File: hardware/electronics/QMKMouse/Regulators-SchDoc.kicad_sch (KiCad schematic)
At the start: 9 parts

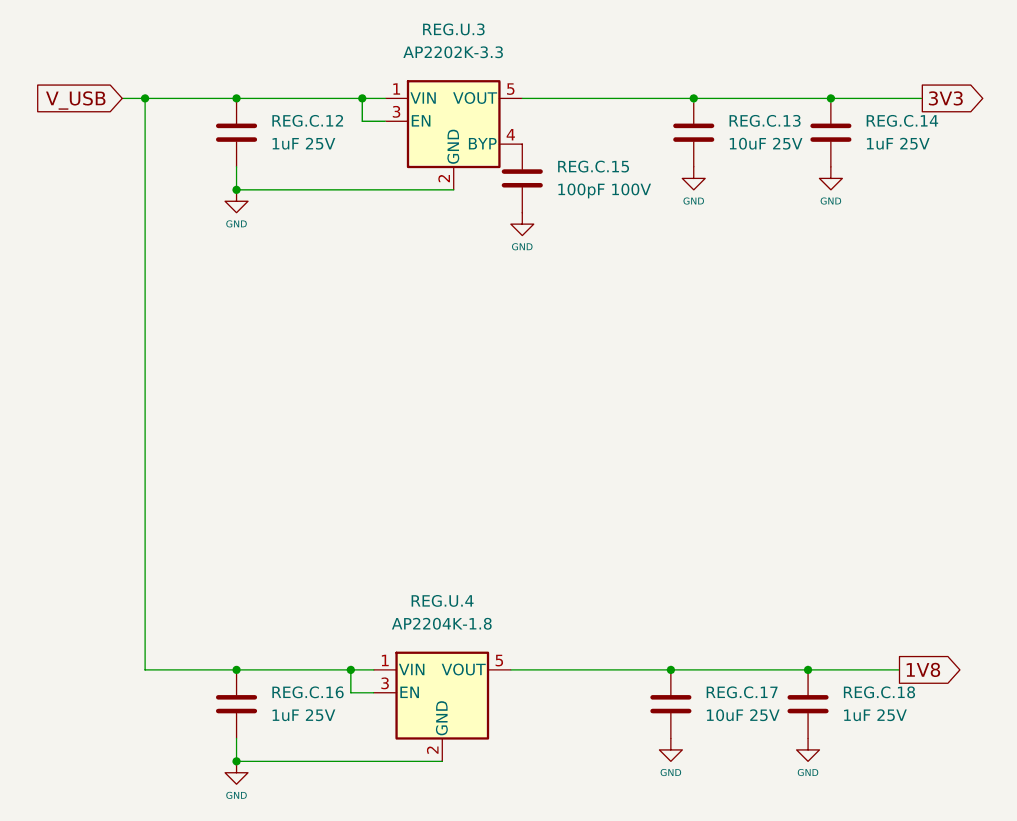
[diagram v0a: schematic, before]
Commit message: update schematic from PCB; sync netlist and fix some symbol orientations; also fix LED symbol
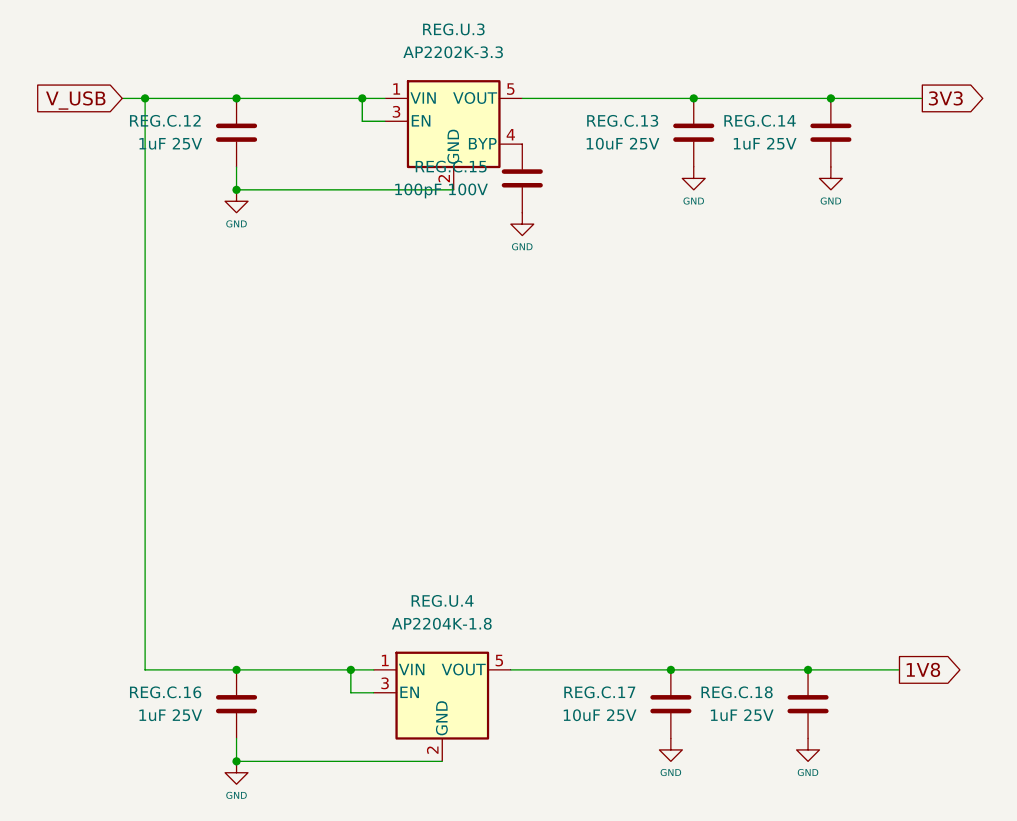
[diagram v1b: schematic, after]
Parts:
- REG.C.12, REG.C.13, REG.C.14, REG.C.15, REG.C.16, REG.C.17, REG.C.18: footprint Capacitor_SMD:C_0805_2012Metric -> Chip_Passives.PcbLib:0805
- REG.U.3: footprint Package_TO_SOT_SMD:SOT-23-5 -> PowerSupply.PcbLib:AP2202 - SOT95P270X145-5N
- REG.U.4: footprint (none) -> PowerSupply.PcbLib:AP2202 - SOT95P270X145-5N
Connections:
- net 1V8: now also REG.C.17.2, REG.C.18.2; no longer REG.C.17.1, REG.C.18.1
- net 3V3: now also REG.C.13.2, REG.C.14.2; no longer REG.C.13.1, REG.C.14.1
- net GND: now also REG.C.12.1, REG.C.13.1, REG.C.14.1, REG.C.15.1, REG.C.16.1, REG.C.17.1, REG.C.18.1; no longer REG.C.12.2, REG.C.13.2, REG.C.14.2, REG.C.15.2, REG.C.16.2, REG.C.17.2, REG.C.18.2
- net V_USB: now also REG.C.12.2, REG.C.16.2; no longer REG.C.12.1, REG.C.16.1
- net at REG.U.3.4 (BYP): now also REG.C.15.2; no longer REG.C.15.1
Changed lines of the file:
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@@
     (pin "1")
   )
-  (symbol (lib_id "Device:C") (at 142.24 72.39 0) (unit 1)
+  (symbol (lib_id "Device:C") (at 142.24 72.39 0) (mirror x) (unit 1)
     (in_bom yes) (on_board yes) (fields_autoplaced)
-    (property "Reference" "REG.C.13" (id 0) (at 146.05 71.1199 0)
-      (effects (font (size 1.27 1.27)) (justify left))
+    (property "Reference" "REG.C.13" (id 0) (at 138.43 71.1199 0)
+      (effects (font (size 1.27 1.27)) (justify right))
     )
-    (property "Value" "10uF 25V" (id 1) (at 146.05 73.6599 0)
-      (effects (font (size 1.27 1.27)) (justify left))
+    (property "Value" "10uF 25V" (id 1) (at 138.43 73.6599 0)
+      (effects (font (size 1.27 1.27)) (justify right))
     )
-    (property "Footprint" "Capacitor_SMD:C_0805_2012Metric" (id 2) (at 143.2052 76.2 0)
+    (property "Footprint" "Chip_Passives.PcbLib:0805" (id 2) (at 143.2052 68.58 0)
       (effects (font (size 1.27 1.27)) hide)
     )
@@
     (pin "2")
   )
-  (symbol (lib_id "Device:C") (at 91.44 135.89 0) (unit 1)
+  (symbol (lib_id "Device:C") (at 91.44 135.89 0) (mirror x) (unit 1)
     (in_bom yes) (on_board yes) (fields_autoplaced)
-    (property "Reference" "REG.C.16" (id 0) (at 95.25 134.6199 0)
-      (effects (font (size 1.27 1.27)) (justify left))
+    (property "Reference" "REG.C.16" (id 0) (at 87.63 134.6199 0)
+      (effects (font (size 1.27 1.27)) (justify right))
     )
-    (property "Value" "1uF 25V" (id 1) (at 95.25 137.1599 0)
-      (effects (font (size 1.27 1.27)) (justify left))
+    (property "Value" "1uF 25V" (id 1) (at 87.63 137.1599 0)
+      (effects (font (size 1.27 1.27)) (justify right))
     )
-    (property "Footprint" "Capacitor_SMD:C_0805_2012Metric" (id 2) (at 92.4052 139.7 0)
+    (property "Footprint" "Chip_Passives.PcbLib:0805" (id 2) (at 92.4052 132.08 0)
       (effects (font (size 1.27 1.27)) hide)
     )
@@
     (pin "2")
   )
-  (symbol (lib_id "Device:C") (at 139.7 135.89 0) (unit 1)
+  (symbol (lib_id "Device:C") (at 139.7 135.89 0) (mirror x) (unit 1)
     (in_bom yes) (on_board yes) (fields_autoplaced)
-    (property "Reference" "REG.C.17" (id 0) (at 143.51 134.6199 0)
-      (effects (font (size 1.27 1.27)) (justify left))
+    (property "Reference" "REG.C.17" (id 0) (at 135.89 134.6199 0)
+      (effects (font (size 1.27 1.27)) (justify right))
     )
-    (property "Value" "10uF 25V" (id 1) (at 143.51 137.1599 0)
-      (effects (font (size 1.27 1.27)) (justify left))
+    (property "Value" "10uF 25V" (id 1) (at 135.89 137.1599 0)
+      (effects (font (size 1.27 1.27)) (justify right))
     )
-    (property "Footprint" "Capacitor_SMD:C_0805_2012Metric" (id 2) (at 140.6652 139.7 0)
+    (property "Footprint" "Chip_Passives.PcbLib:0805" (id 2) (at 140.6652 132.08 0)
       (effects (font (size 1.27 1.27)) hide)
     )
@@
     (property "Reference" "REG.U.3" (id 0) (at 115.57 60.96 0))
     (property "Value" "AP2202K-3.3" (id 1) (at 115.57 63.5 0))
-    (property "Footprint" "Package_TO_SOT_SMD:SOT-23-5" (id 2) (at 115.57 62.865 0)
+    (property "Footprint" "PowerSupply.PcbLib:AP2202 - SOT95P270X145-5N" (id 2) (at 115.57 62.865 0)
       (effects (font (size 1.27 1.27)) hide)
     )
@@
     (pin "5")
   )
-  (symbol (lib_id "Device:C") (at 154.94 135.89 0) (unit 1)
+  (symbol (lib_id "Device:C") (at 154.94 135.89 0) (mirror x) (unit 1)
     (in_bom yes) (on_board yes) (fields_autoplaced)
-    (property "Reference" "REG.C.18" (id 0) (at 158.75 134.6199 0)
-      (effects (font (size 1.27 1.27)) (justify left))
+    (property "Reference" "REG.C.18" (id 0) (at 151.13 134.6199 0)
+      (effects (font (size 1.27 1.27)) (justify right))
     )
-    (property "Value" "1uF 25V" (id 1) (at 158.75 137.1599 0)
-      (effects (font (size 1.27 1.27)) (justify left))
+    (property "Value" "1uF 25V" (id 1) (at 151.13 137.1599 0)
+      (effects (font (size 1.27 1.27)) (justify right))
     )
-    (property "Footprint" "Capacitor_SMD:C_0805_2012Metric" (id 2) (at 155.9052 139.7 0)
+    (property "Footprint" "Chip_Passives.PcbLib:0805" (id 2) (at 155.9052 132.08 0)
       (effects (font (size 1.27 1.27)) hide)
     )
@@
     (pin "2")
   )
-  (symbol (lib_id "Device:C") (at 157.48 72.39 0) (unit 1)
+  (symbol (lib_id "Device:C") (at 157.48 72.39 0) (mirror x) (unit 1)
     (in_bom yes) (on_board yes) (fields_autoplaced)
-    (property "Reference" "REG.C.14" (id 0) (at 161.29 71.1199 0)
-      (effects (font (size 1.27 1.27)) (justify left))
+    (property "Reference" "REG.C.14" (id 0) (at 153.67 71.1199 0)
+      (effects (font (size 1.27 1.27)) (justify right))
     )
-    (property "Value" "1uF 25V" (id 1) (at 161.29 73.6599 0)
-      (effects (font (size 1.27 1.27)) (justify left))
+    (property "Value" "1uF 25V" (id 1) (at 153.67 73.6599 0)
+      (effects (font (size 1.27 1.27)) (justify right))
     )
-    (property "Footprint" "Capacitor_SMD:C_0805_2012Metric" (id 2) (at 158.4452 76.2 0)
+    (property "Footprint" "Chip_Passives.PcbLib:0805" (id 2) (at 158.4452 68.58 0)
       (effects (font (size 1.27 1.27)) hide)
     )
@@
     (pin "2")
   )
-  (symbol (lib_id "Device:C") (at 123.19 77.47 0) (unit 1)
+  (symbol (lib_id "Device:C") (at 123.19 77.47 0) (mirror x) (unit 1)
     (in_bom no) (on_board yes) (fields_autoplaced)
-    (property "Reference" "REG.C.15" (id 0) (at 127 76.1999 0)
-      (effects (font (size 1.27 1.27)) (justify left))
+    (property "Reference" "REG.C.15" (id 0) (at 119.38 76.1999 0)
+      (effects (font (size 1.27 1.27)) (justify right))
     )
-    (property "Value" "100pF 100V" (id 1) (at 127 78.7399 0)
-      (effects (font (size 1.27 1.27)) (justify left))
+    (property "Value" "100pF 100V" (id 1) (at 119.38 78.7399 0)
+      (effects (font (size 1.27 1.27)) (justify right))
     )
-    (property "Footprint" "Capacitor_SMD:C_0805_2012Metric" (id 2) (at 124.1552 81.28 0)
+    (property "Footprint" "Chip_Passives.PcbLib:0805" (id 2) (at 124.1552 73.66 0)
       (effects (font (size 1.27 1.27)) hide)
     )
@@
     (pin "2")
   )
-  (symbol (lib_id "Device:C") (at 91.44 72.39 0) (unit 1)
+  (symbol (lib_id "Device:C") (at 91.44 72.39 0) (mirror x) (unit 1)
     (in_bom yes) (on_board yes) (fields_autoplaced)
-    (property "Reference" "REG.C.12" (id 0) (at 95.25 71.1199 0)
-      (effects (font (size 1.27 1.27)) (justify left))
+    (property "Reference" "REG.C.12" (id 0) (at 87.63 71.1199 0)
+      (effects (font (size 1.27 1.27)) (justify right))
     )
-    (property "Value" "1uF 25V" (id 1) (at 95.25 73.6599 0)
-      (effects (font (size 1.27 1.27)) (justify left))
+    (property "Value" "1uF 25V" (id 1) (at 87.63 73.6599 0)
+      (effects (font (size 1.27 1.27)) (justify right))
     )
-    (property "Footprint" "Capacitor_SMD:C_0805_2012Metric" (id 2) (at 92.4052 76.2 0)
+    (property "Footprint" "Chip_Passives.PcbLib:0805" (id 2) (at 92.4052 68.58 0)
       (effects (font (size 1.27 1.27)) hide)
     )
@@
     (property "Reference" "REG.U.4" (id 0) (at 114.3 124.46 0))
     (property "Value" "AP2204K-1.8" (id 1) (at 114.3 127 0))
-    (property "Footprint" "" (id 2) (at 114.3 126.365 0)
+    (property "Footprint" "PowerSupply.PcbLib:AP2202 - SOT95P270X145-5N" (id 2) (at 114.3 126.365 0)
       (effects (font (size 1.27 1.27)) hide)
     )
